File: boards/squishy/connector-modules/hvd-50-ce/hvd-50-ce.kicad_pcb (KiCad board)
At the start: 6 copper layers, 84.8 x 34 mm, 20 parts, among them J1 SCSI PHY Mezz, J3 Conn_01x04, J5 112-050-213R001, U1 M24C02-RMC

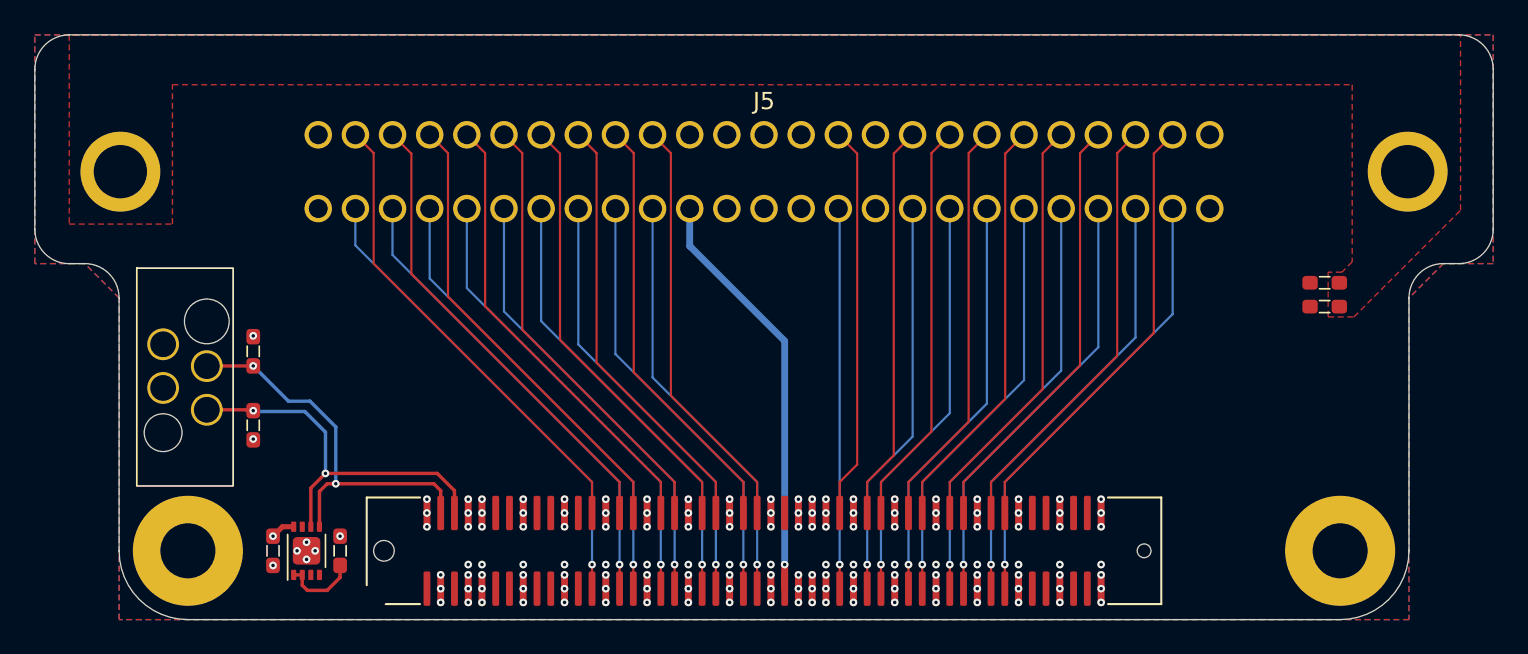
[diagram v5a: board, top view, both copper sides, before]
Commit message: squishy: connectors: re-routed the hvd-50-ce board
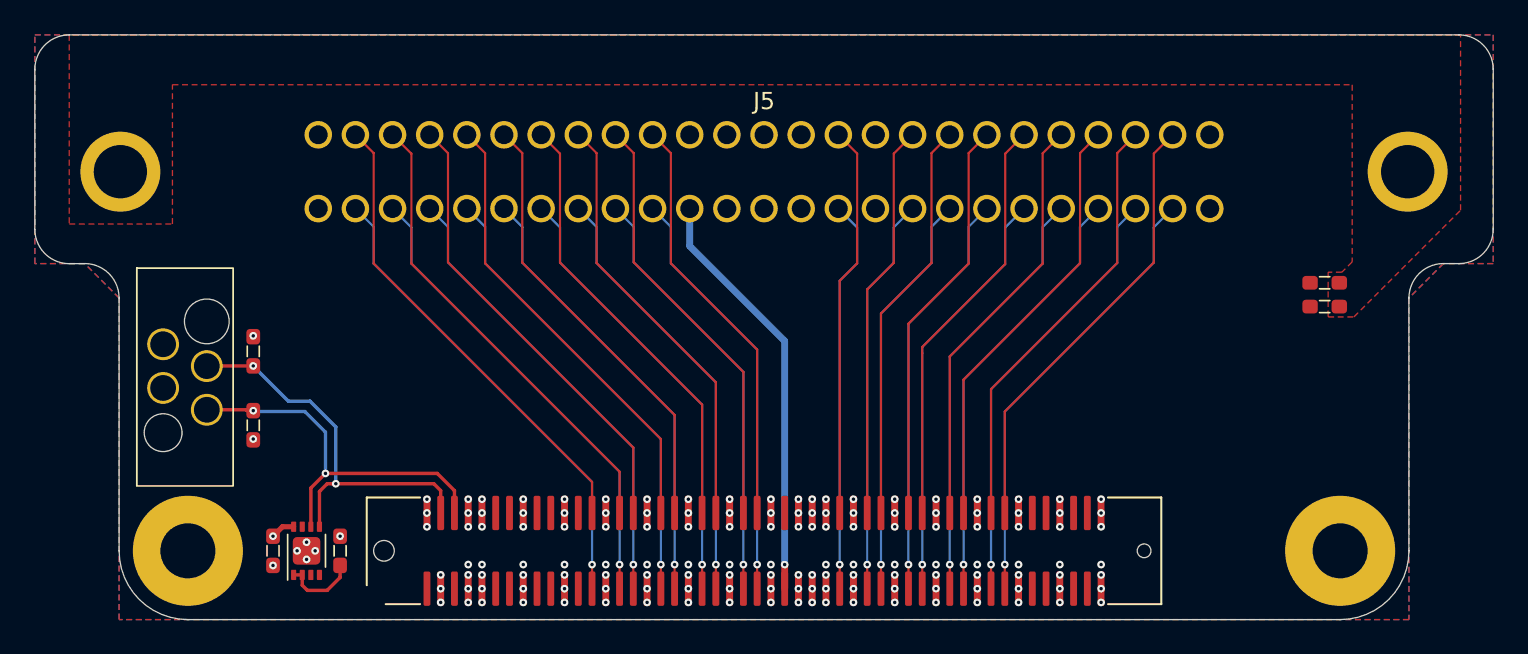
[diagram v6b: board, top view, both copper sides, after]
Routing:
- net /CON.ATN+: track 22.1 -> 23.0 mm
